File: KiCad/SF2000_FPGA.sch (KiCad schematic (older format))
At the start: 10 parts, among them J3 Conn_02x03_Odd_Even, J4 Conn_02x01, J8 Conn_02x01, J9 Conn_02x01, U7 10M04SCE144

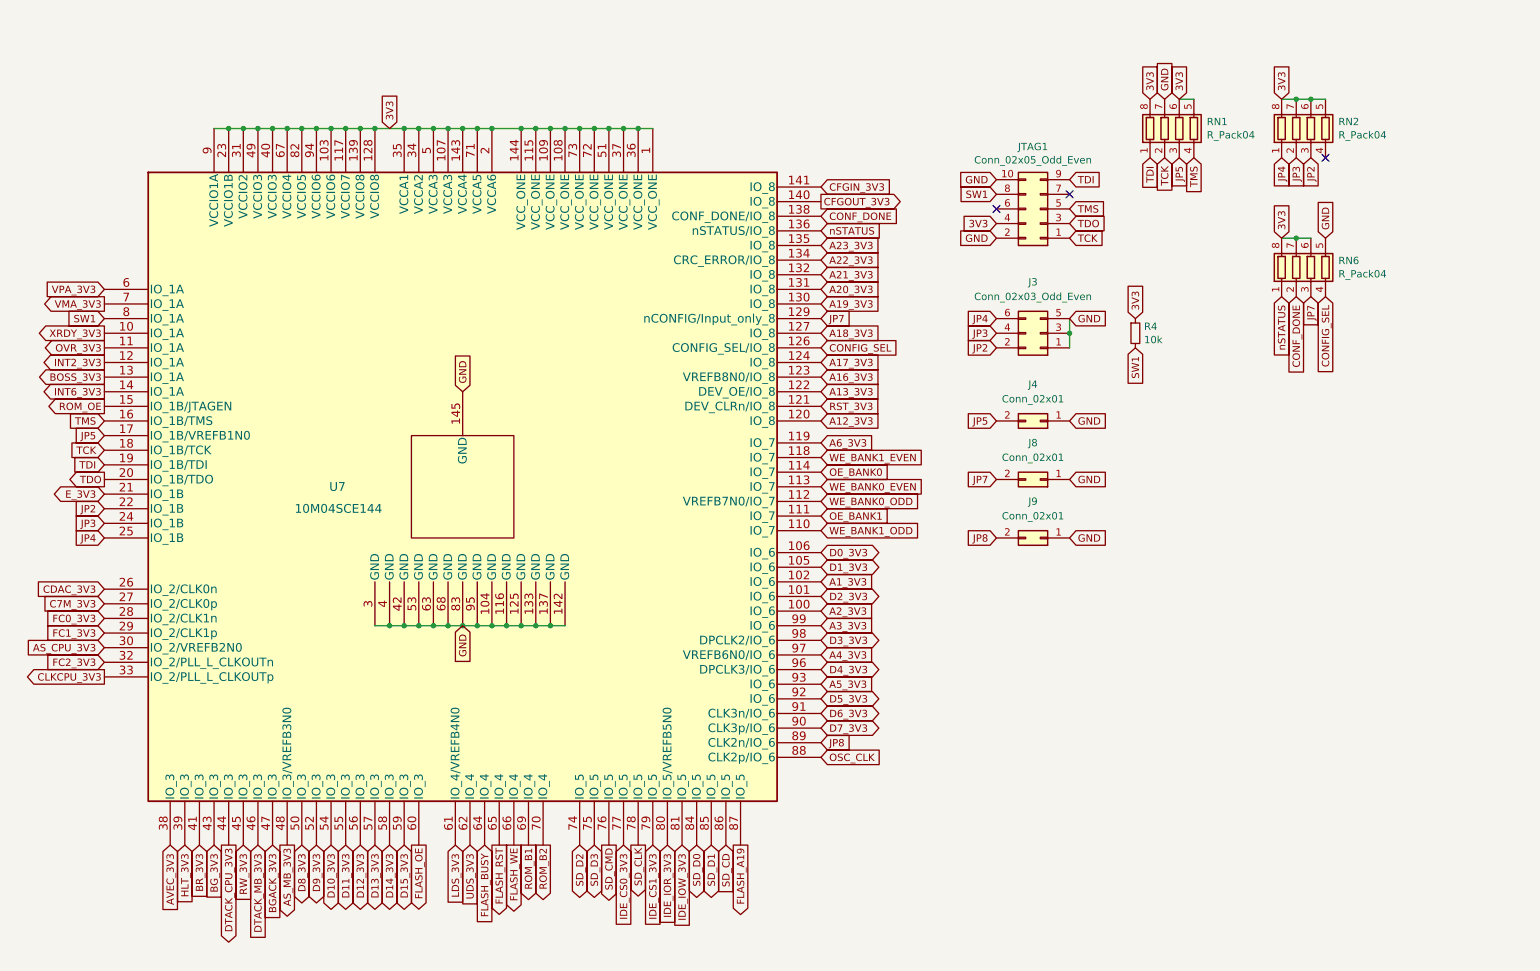
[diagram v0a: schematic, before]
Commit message: fixed JP6
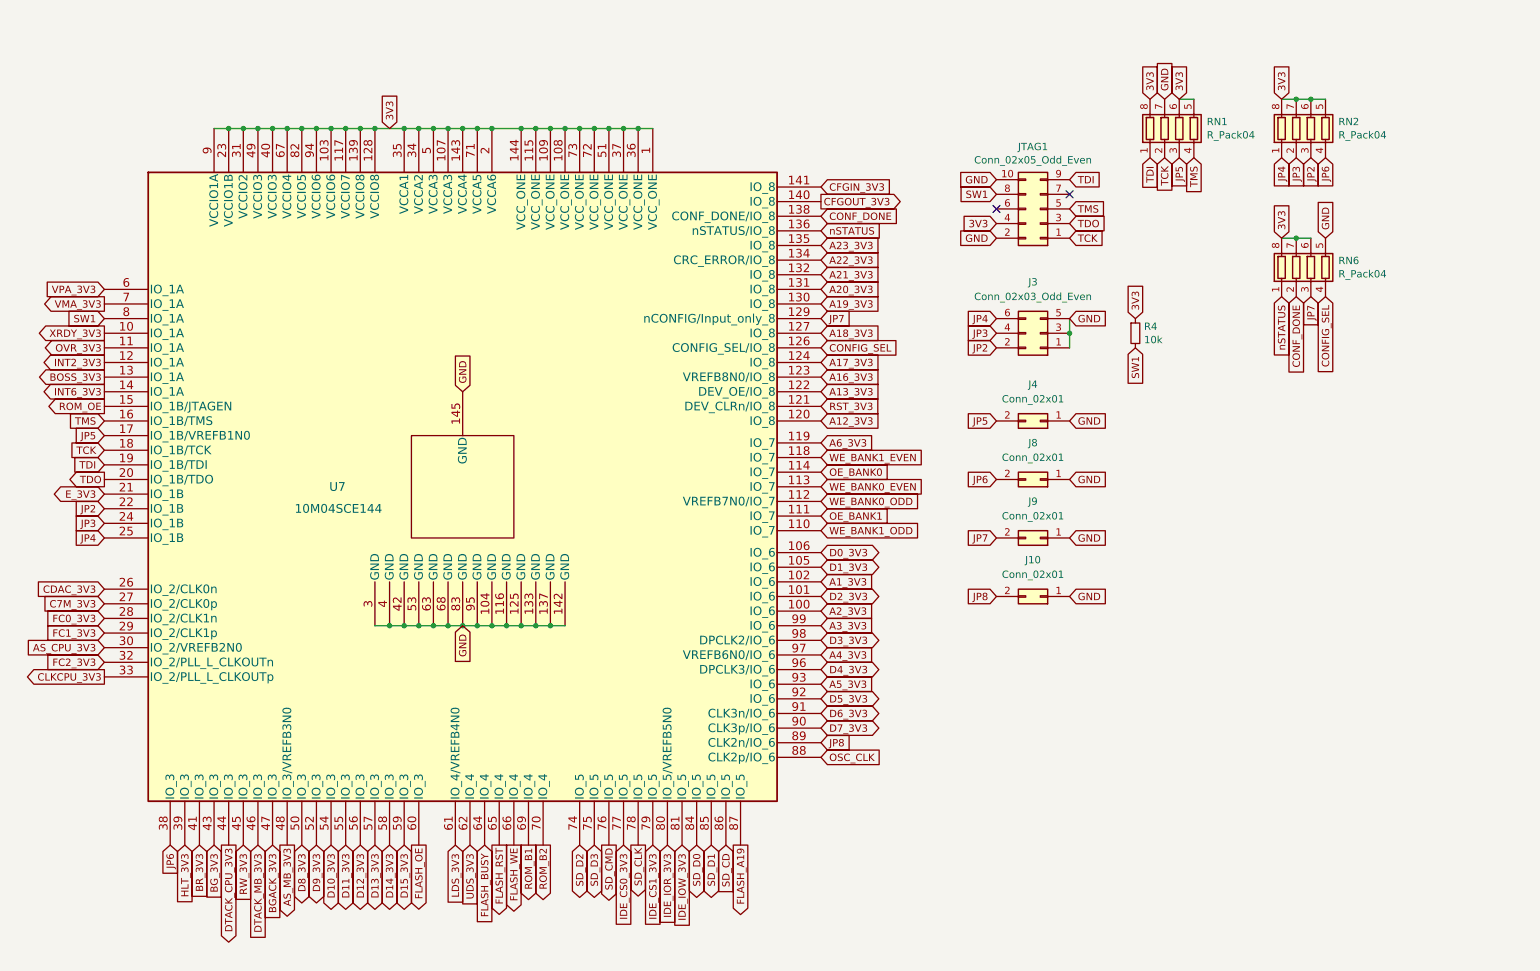
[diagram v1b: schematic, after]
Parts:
- added J8: Conn_02x01, Connector_PinHeader_2.00mm:PinHeader_2x01_P2.00mm_Vertical, symbol Connector_Generic:Conn_02x01
- renumbered J9 to J10, J8 to J9
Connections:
- net AVEC_3V3 is gone; now on net JP6: U7.38 (IO_3)
- net GND: now also J8.1 (Pin_1)
- net JP6: now reaches RN2.4 (R4.1)
- net JP6: now also J8.2 (Pin_2)
- no-connect marks 3 -> 2
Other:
- moved on the sheet: J10, J9
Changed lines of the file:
@@
 Text GLabel 2300 6000 3    50   Input ~ 0
 RW_3V3
-Text GLabel 1800 6000 3    50   Input ~ 0
-AVEC_3V3
 Text GLabel 6250 2900 2    50   Input ~ 0
 A13_3V3
@@
 Wire Wire Line
 	7950 2500 7950 2600
-NoConn ~ 9700 1300
 Text GLabel 7950 2400 2    50   Input ~ 0
 GND
@@
 JP7
 $Comp
-L Connector_Generic:Conn_02x01 J8
+L Connector_Generic:Conn_02x01 J9
 U 1 1 62127717
-P 7750 3500
-F 0 "J8" H 7800 3250 50  0000 C CNN
-F 1 "Conn_02x01" H 7800 3350 50  0000 C CNN
-F 2 "Connector_PinHeader_2.00mm:PinHeader_2x01_P2.00mm_Vertical" H 7750 3500 50  0001 C CNN
-F 3 "~" H 7750 3500 50  0001 C CNN
-	1    7750 3500
-	-1   0    0    1
-$EndComp
-Text GLabel 7950 3500 2    50   Input ~ 0
-GND
-Text GLabel 7450 3500 0    50   Input ~ 0
-JP7
-$Comp
-L Connector_Generic:Conn_02x01 J9
-U 1 1 62132436
 P 7750 3900
 F 0 "J9" H 7800 3650 50  0000 C CNN
@@
 GND
 Text GLabel 7450 3900 0    50   Input ~ 0
+JP7
+$Comp
+L Connector_Generic:Conn_02x01 J10
+U 1 1 62132436
+P 7750 4300
+F 0 "J10" H 7800 4050 50  0000 C CNN
+F 1 "Conn_02x01" H 7800 4150 50  0000 C CNN
+F 2 "Connector_PinHeader_2.00mm:PinHeader_2x01_P2.00mm_Vertical" H 7750 4300 50  0001 C CNN
+F 3 "~" H 7750 4300 50  0001 C CNN
+	1    7750 4300
+	-1   0    0    1
+$EndComp
+Text GLabel 7950 4300 2    50   Input ~ 0
+GND
+Text GLabel 7450 4300 0    50   Input ~ 0
 JP8
 Text GLabel 6250 5300 2    50   Input ~ 0
@@
 Text GLabel 9600 2250 3    50   Input ~ 0
 JP7
+Text GLabel 7450 3500 0    50   Input ~ 0
+JP6
+$Comp
+L Connector_Generic:Conn_02x01 J8
+U 1 1 621772F2
+P 7750 3500
+F 0 "J8" H 7800 3250 50  0000 C CNN
+F 1 "Conn_02x01" H 7800 3350 50  0000 C CNN
+F 2 "Connector_PinHeader_2.00mm:PinHeader_2x01_P2.00mm_Vertical" H 7750 3500 50  0001 C CNN
+F 3 "~" H 7750 3500 50  0001 C CNN
+	1    7750 3500
+	-1   0    0    1
+$EndComp
+Text GLabel 7950 3500 2    50   Input ~ 0
+GND
+Text GLabel 9700 1300 3    50   Input ~ 0
+JP6
+Text GLabel 1800 6000 3    50   Input ~ 0
+JP6
 $EndSCHEMATC

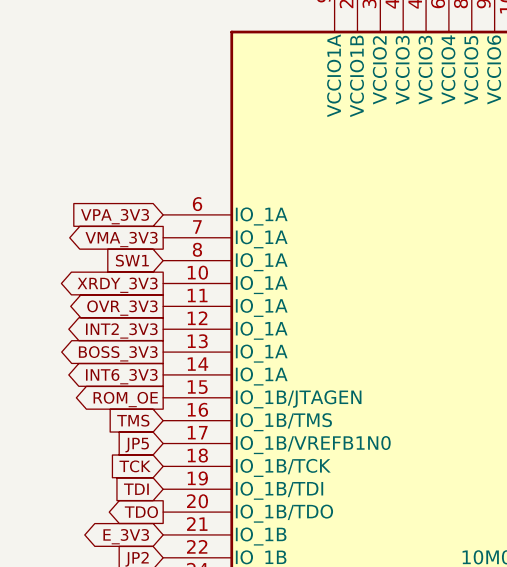
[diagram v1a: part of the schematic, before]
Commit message: added ROM_WE signal/pin to FPGA, removed XRDY-signal/pin, and some silkscreen fixes
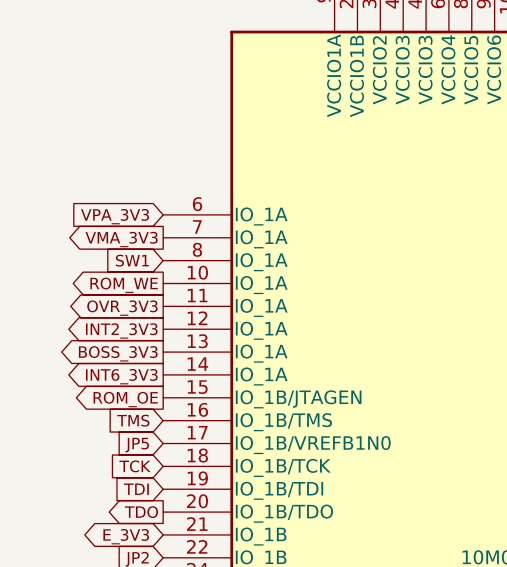
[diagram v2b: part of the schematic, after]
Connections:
- net XRDY_3V3 renamed ROM_WE
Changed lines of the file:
@@
 CDAC_3V3
 Text GLabel 1350 2500 0    50   Output ~ 0
-XRDY_3V3
+ROM_WE
 Text GLabel 1350 2600 0    50   Output ~ 0
 OVR_3V3

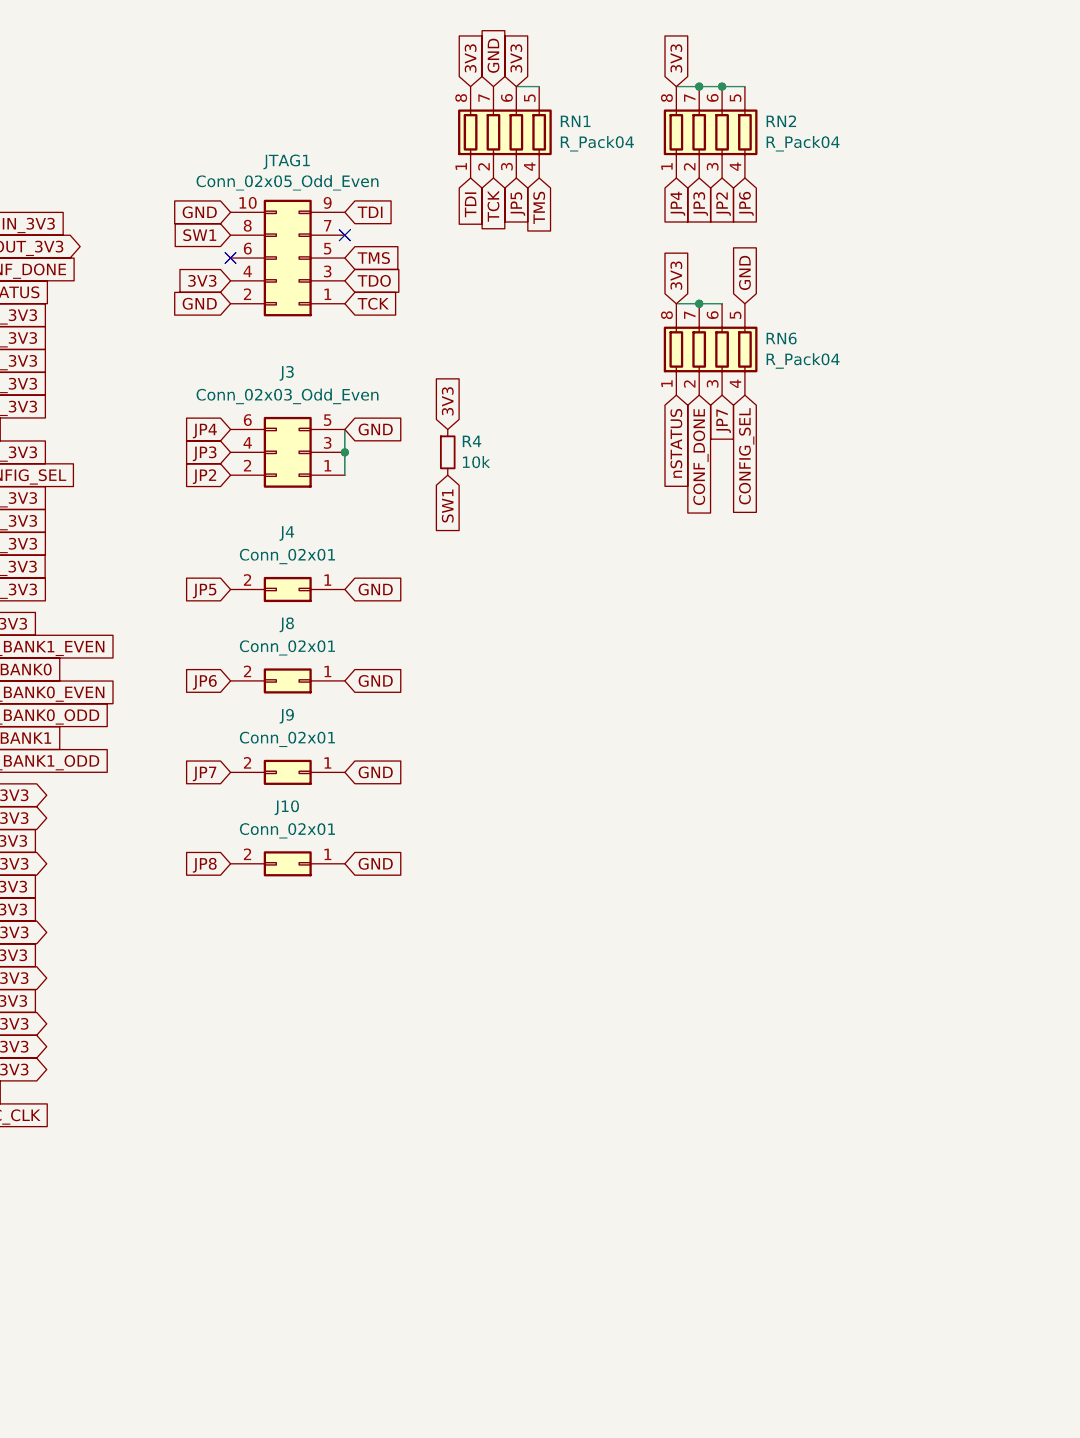
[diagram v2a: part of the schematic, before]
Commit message: added RC-debounce circuit for SW1
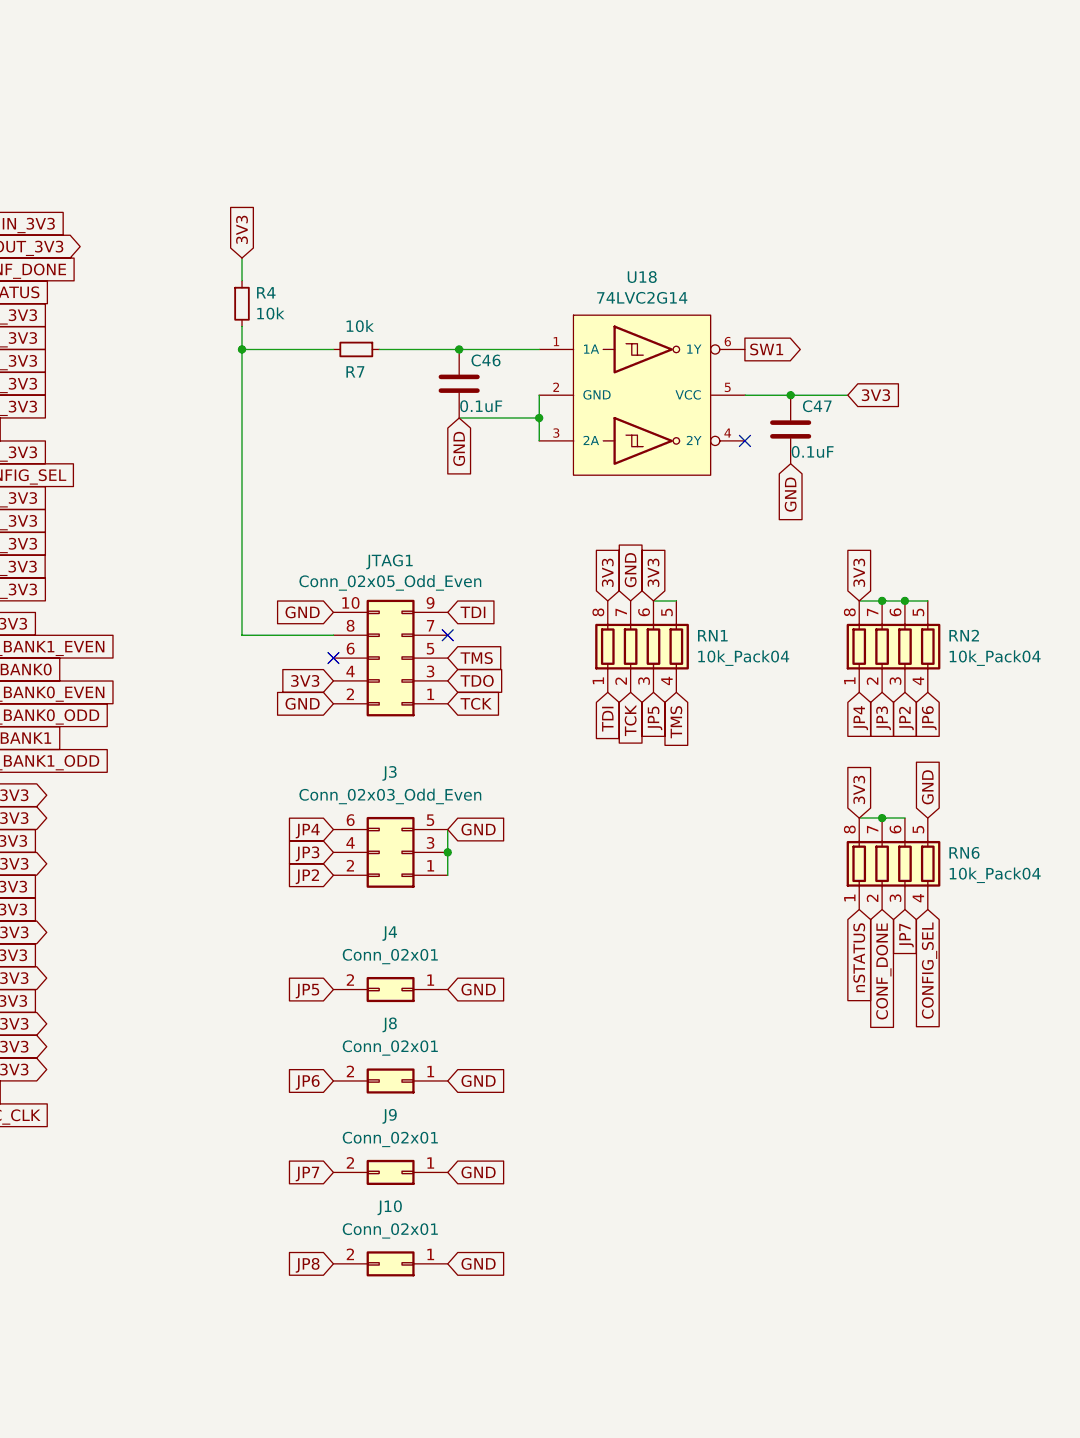
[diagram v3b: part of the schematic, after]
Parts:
- added C46, C47: 0.1uF, Capacitor_SMD:C_0805_2012Metric_Pad1.15x1.40mm_HandSolder, symbol Device:C
- added R7: 10k, Resistor_SMD:R_0805_2012Metric_Pad1.15x1.40mm_HandSolder, symbol Device:R_Small
- added U18: 74LVC2G14, Package_SO:TSOP-6_1.65x3.05mm_P0.95mm, symbol SF2000:74LVC2G14
- RN1, RN2, RN6: value R_Pack04 -> 10k_Pack04
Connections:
- net 3V3: now also C47.1, U18.5 (VCC)
- net GND: now also C46.2, C47.2, U18.2 (GND), U18.3 (2A)
- net SW1: now also U18.6 (1Y); no longer JTAG1.8 (Pin_8), R4.2
- new net: C46.1, R7.1, U18.1 (1A)
- new net: JTAG1.8 (Pin_8), R4.2, R7.2
- no-connect marks 2 -> 3
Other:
- moved on the sheet: J10, J3, J4, J8, J9, JTAG1, RN1, RN2, RN6
